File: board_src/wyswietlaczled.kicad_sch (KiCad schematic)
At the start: 19 parts, among them J24 Conn_01x08, J25 Conn_01x04, Q2 SS8550, Q3 SS8550, Q4 SS8550, Q5 SS8550

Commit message: wersja 3d
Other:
- note added: "Wartości rezystorów?"
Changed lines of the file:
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@@
 	(generator_version "9.0")
 	(paper "A4")
+	(text "Wartości rezystorów?"
+		(exclude_from_sim no)
+		(at 129.54 126.238 0)
+		(effects
+			(font
+				(size 1.27 1.27)
+			)
+		)
+	)
+	(text "Wartości rezystorów?"
+		(exclude_from_sim no)
+		(at 142.748 67.564 0)
+		(effects
+			(font
+				(size 1.27 1.27)
+			)
+		)
+	)
 	(text "DIGIT"
 		(exclude_from_sim no)
@@
 	(text "wspólna anoda\n"
 		(exclude_from_sim no)
-		(at 132.08 59.69 0)
+		(at 119.888 66.548 0)
 		(effects
 			(font

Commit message: wersja z FT232RN
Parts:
- R31, R32, R33, R34: value 103 -> 10k
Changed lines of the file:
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@@
 			)
 		)
-		(property "Value" "103"
+		(property "Value" "10k"
 			(at 111.76 125.476 90)
 			(effects
@@
 			)
 		)
-		(property "Value" "103"
+		(property "Value" "10k"
 			(at 114.3 125.476 90)
 			(effects
@@
 			)
 		)
-		(property "Value" "103"
+		(property "Value" "10k"
 			(at 109.22 125.476 90)
 			(effects
@@
 			)
 		)
-		(property "Value" "103"
+		(property "Value" "10k"
 			(at 106.68 125.476 90)
 			(effects

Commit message: Wersja ze sciezkami miedzianymi
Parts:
- R13, R24, R25, R26, R27, R28, R29, R30, R31, R32, R33, R34: footprint Resistor_SMD:R_0201_0603Metric -> Resistor_SMD:R_0603_1608Metric
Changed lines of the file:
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@@
 			)
 		)
-		(property "Footprint" "Resistor_SMD:R_0201_0603Metric"
+		(property "Footprint" "Resistor_SMD:R_0603_1608Metric"
 			(at 140.97 88.138 90)
 			(effects
@@
 			)
 		)
-		(property "Footprint" "Resistor_SMD:R_0201_0603Metric"
+		(property "Footprint" "Resistor_SMD:R_0603_1608Metric"
 			(at 140.97 83.058 90)
 			(effects
@@
 			)
 		)
-		(property "Footprint" "Resistor_SMD:R_0201_0603Metric"
+		(property "Footprint" "Resistor_SMD:R_0603_1608Metric"
 			(at 116.078 125.73 90)
 			(effects
@@
 			)
 		)
-		(property "Footprint" "Resistor_SMD:R_0201_0603Metric"
+		(property "Footprint" "Resistor_SMD:R_0603_1608Metric"
 			(at 140.97 85.598 90)
 			(effects
@@
 			)
 		)
-		(property "Footprint" "Resistor_SMD:R_0201_0603Metric"
+		(property "Footprint" "Resistor_SMD:R_0603_1608Metric"
 			(at 118.618 125.73 90)
 			(effects
@@
 			)
 		)
-		(property "Footprint" "Resistor_SMD:R_0201_0603Metric"
+		(property "Footprint" "Resistor_SMD:R_0603_1608Metric"
 			(at 140.97 90.678 90)
 			(effects
@@
 			)
 		)
-		(property "Footprint" "Resistor_SMD:R_0201_0603Metric"
+		(property "Footprint" "Resistor_SMD:R_0603_1608Metric"
 			(at 140.97 80.518 90)
 			(effects
@@
 			)
 		)
-		(property "Footprint" "Resistor_SMD:R_0201_0603Metric"
+		(property "Footprint" "Resistor_SMD:R_0603_1608Metric"
 			(at 140.97 75.438 90)
 			(effects
@@
 			)
 		)
-		(property "Footprint" "Resistor_SMD:R_0201_0603Metric"
+		(property "Footprint" "Resistor_SMD:R_0603_1608Metric"
 			(at 140.97 72.898 90)
 			(effects
@@
 			)
 		)
-		(property "Footprint" "Resistor_SMD:R_0201_0603Metric"
+		(property "Footprint" "Resistor_SMD:R_0603_1608Metric"
 			(at 140.97 77.978 90)
 			(effects
@@
 			)
 		)
-		(property "Footprint" "Resistor_SMD:R_0201_0603Metric"
+		(property "Footprint" "Resistor_SMD:R_0603_1608Metric"
 			(at 113.538 125.73 90)
 			(effects
@@
 			)
 		)
-		(property "Footprint" "Resistor_SMD:R_0201_0603Metric"
+		(property "Footprint" "Resistor_SMD:R_0603_1608Metric"
 			(at 110.998 125.73 90)
 			(effects

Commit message: najnowsza wersja
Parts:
- R13, R24, R25, R26, R27, R28, R29, R30: value 221 -> 220
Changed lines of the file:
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@@
 			)
 		)
-		(property "Value" "221"
+		(property "Value" "220"
 			(at 141.224 83.82 90)
 			(effects
@@
 			)
 		)
-		(property "Value" "221"
+		(property "Value" "220"
 			(at 141.224 78.74 90)
 			(effects
@@
 			)
 		)
-		(property "Value" "221"
+		(property "Value" "220"
 			(at 141.224 81.28 90)
 			(effects
@@
 			)
 		)
-		(property "Value" "221"
+		(property "Value" "220"
 			(at 141.224 86.36 90)
 			(effects
@@
 			)
 		)
-		(property "Value" "221"
+		(property "Value" "220"
 			(at 141.224 76.2 90)
 			(effects
@@
 			)
 		)
-		(property "Value" "221"
+		(property "Value" "220"
 			(at 141.224 71.12 90)
 			(effects
@@
 			)
 		)
-		(property "Value" "221"
+		(property "Value" "220"
 			(at 141.224 68.58 90)
 			(effects
@@
 			)
 		)
-		(property "Value" "221"
+		(property "Value" "220"
 			(at 141.224 73.66 90)
 			(effects
@@
 					(size 1.27 1.27)
 				)
-				(hide yes)
-			)
-		)
+			)
+		)

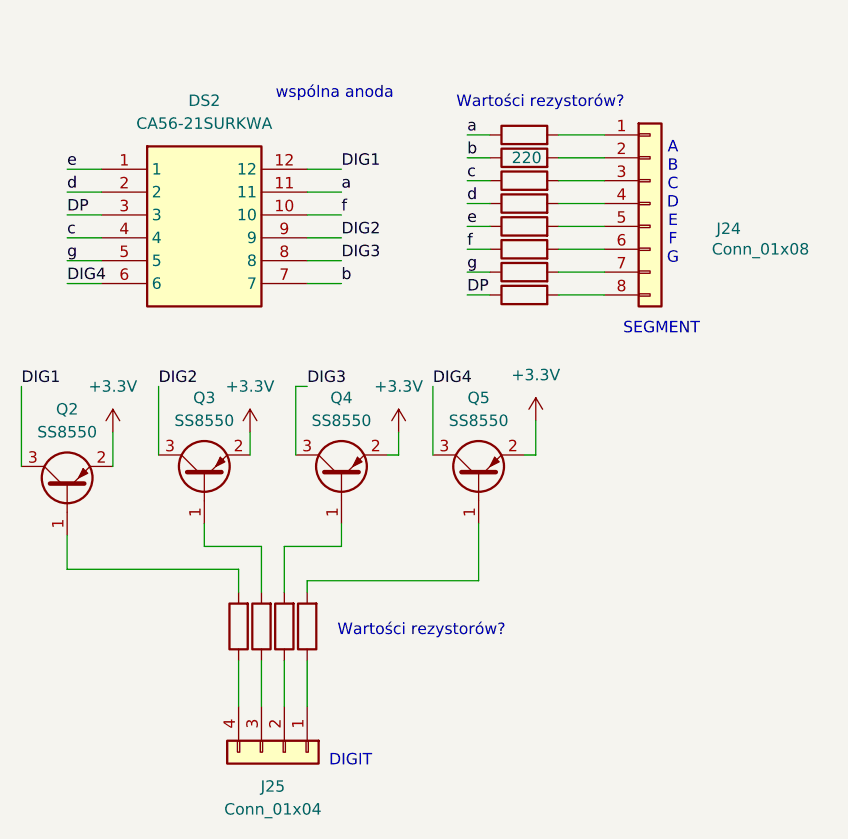
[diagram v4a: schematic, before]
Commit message: Poprawki w schematach. Rozpoczęte korekty płytki
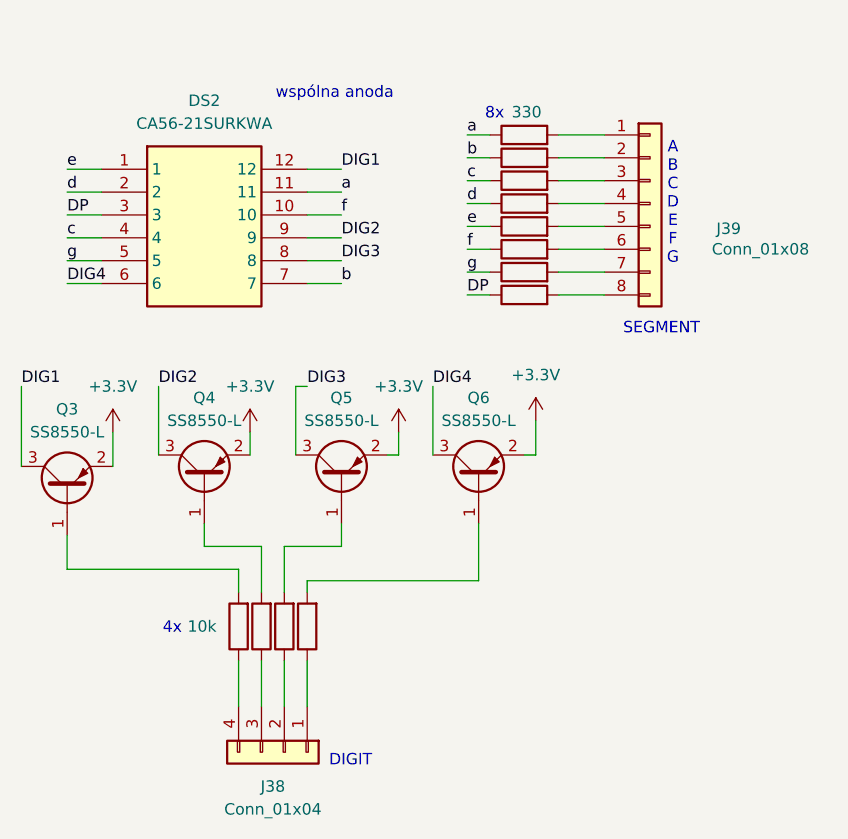
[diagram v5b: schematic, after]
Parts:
- Q3: renamed from Q2; value SS8550 -> SS8550-L; footprint Package_TO_SOT_SMD:SOT-23 -> Package_TO_SOT_SMD:SOT-23_Handsoldering
- Q4: renamed from Q3; value SS8550 -> SS8550-L; footprint Package_TO_SOT_SMD:SOT-23 -> Package_TO_SOT_SMD:SOT-23_Handsoldering
- Q5: renamed from Q4; value SS8550 -> SS8550-L; footprint Package_TO_SOT_SMD:SOT-23 -> Package_TO_SOT_SMD:SOT-23_Handsoldering
- Q6: renamed from Q5; value SS8550 -> SS8550-L; footprint Package_TO_SOT_SMD:SOT-23 -> Package_TO_SOT_SMD:SOT-23_Handsoldering
- R39: renamed from R31; footprint Resistor_SMD:R_0603_1608Metric -> Resistor_SMD:R_0603_1608Metric_Pad0.98x0.95mm_HandSolder
- R40: renamed from R32; footprint Resistor_SMD:R_0603_1608Metric -> Resistor_SMD:R_0603_1608Metric_Pad0.98x0.95mm_HandSolder
- R41: renamed from R33; footprint Resistor_SMD:R_0603_1608Metric -> Resistor_SMD:R_0603_1608Metric_Pad0.98x0.95mm_HandSolder
- R42: renamed from R34; footprint Resistor_SMD:R_0603_1608Metric -> Resistor_SMD:R_0603_1608Metric_Pad0.98x0.95mm_HandSolder
- R43: renamed from R13; value 220 -> 330; footprint Resistor_SMD:R_0603_1608Metric -> Resistor_SMD:R_0603_1608Metric_Pad0.98x0.95mm_HandSolder
- R44: renamed from R24; footprint Resistor_SMD:R_0603_1608Metric -> Resistor_SMD:R_0603_1608Metric_Pad0.98x0.95mm_HandSolder
- R45: renamed from R25; value 220 -> 330; footprint Resistor_SMD:R_0603_1608Metric -> Resistor_SMD:R_0603_1608Metric_Pad0.98x0.95mm_HandSolder
- R46: renamed from R26; value 220 -> 330; footprint Resistor_SMD:R_0603_1608Metric -> Resistor_SMD:R_0603_1608Metric_Pad0.98x0.95mm_HandSolder
- R47: renamed from R27; value 220 -> 330; footprint Resistor_SMD:R_0603_1608Metric -> Resistor_SMD:R_0603_1608Metric_Pad0.98x0.95mm_HandSolder
- R48: renamed from R28; value 220 -> 330; footprint Resistor_SMD:R_0603_1608Metric -> Resistor_SMD:R_0603_1608Metric_Pad0.98x0.95mm_HandSolder
- R49: renamed from R29; value 220 -> 330; footprint Resistor_SMD:R_0603_1608Metric -> Resistor_SMD:R_0603_1608Metric_Pad0.98x0.95mm_HandSolder
- R50: renamed from R30; value 220 -> 330; footprint Resistor_SMD:R_0603_1608Metric -> Resistor_SMD:R_0603_1608Metric_Pad0.98x0.95mm_HandSolder
- renumbered J25 to J38, J24 to J39
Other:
- note added: "4x"
- note added: "8x"
- note removed: "Wartości rezystorów?"
